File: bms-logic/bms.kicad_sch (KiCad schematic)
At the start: 63 parts, among them J4 Conn_02x07_Odd_Even, Q1 PBSS4350T,215, Q2 BSS123, Q3 DMZ6012E, Q4 DMZ6012E, U11 A2001WR-S-12PD01, U12 A2001WR-S-08PD01, U2 BQ76972PFBR, U3 2SC2383_C41375137, U4 XC6206P332MR

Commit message: started afe layout
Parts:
- removed D6: SMCJ64CA, PCM_JLCPCB:D_SMC, symbol PCM_JLCPCB-Diodes:TVS-Bi,SMCJ64CA
- added D16, D17: BZT52C75, PCM_JLCPCB:D_SOD-123, symbol PCM_JLCPCB-Diodes:Zener,BZT52C75
- renumbered C14 to C10, C15 to C11, C16 to C12, C17 to C13, C18 to C14, C19 to C15, C20 to C16, C7 to C3, C8 to C4, C9 to C5, C10 to C6, C11 to C7, C12 to C8, C13 to C9, J4 to J2, U11 to U2, U12 to U3, U2 to U4, U3 to U5, U4 to U6
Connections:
- net AFE_BAT: now also D16.1
- net GND: now also D17.1
- new net: D16.2, D17.2
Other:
- removed sheet BALANCE
- removed sheet BALANCE1
- added sheet BALANCE15 (balance.kicad_sch)
- added sheet BALANCE16 (balance.kicad_sch)

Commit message: isolated comms
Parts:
- removed U2: A2001WR-S-12PD01, JLCImport:A2001WR-S-12PD01, symbol JLCImport:A2001WR-S-12PD01
- removed U3: A2001WR-S-08PD01, JLCImport:A2001WR-S-08PD01, symbol JLCImport:A2001WR-S-08PD01
- added CN1: S12B-ZR-SM4A-TF, Connector_JST:JST_ZH_S12B-ZR-SM4A-TF_1x12-1MP_P1.50mm_Horizontal, symbol JLCImport:S12B-ZR-SM4A-TF
- added U2: S8B-ZR-SM4A-TF_LF_SN, Connector_JST:JST_ZH_S8B-ZR-SM4A-TF_1x08-1MP_P1.50mm_Horizontal, symbol JLCImport:S8B-ZR-SM4A-TF_LF_SN
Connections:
- net Cell0: now also CN1.2
- net Cell1: now also U2.1
- net Cell10: now also CN1.7
- net Cell11: now also U2.6
- net Cell12: now also CN1.8
- net Cell13: now also U2.7
- net Cell14: now also CN1.9
- net Cell15: now also U2.8
- net Cell16: now also CN1.10
- net Cell2: now also CN1.3
- net Cell3: now also U2.2
- net Cell4: now also CN1.4
- net Cell5: now also U2.3
- net Cell6: now also CN1.5
- net Cell7: now also U2.4
- net Cell8: now also CN1.6
- net Cell9: now also U2.5
- net GND: now also CN1.1, CN1.13, CN1.14, U2.10, U2.9
- net TOP_CELL: now also CN1.11
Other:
- note added: "make these smaller"

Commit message: diagonal
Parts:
- CN1: footprint Connector_JST:JST_ZH_S12B-ZR-SM4A-TF_1x12-1MP_P1.50mm_Horizontal -> JLCImport:JST_ZH_S12B-ZR-SM4A-TF_1x12-1MP_P1.50mm_Horizontal
- U2: footprint Connector_JST:JST_ZH_S8B-ZR-SM4A-TF_1x08-1MP_P1.50mm_Horizontal -> JLCImport:JST_ZH_S8B-ZR-SM4A-TF_1x08-1MP_P1.50mm_Horizontal
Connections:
- net Cell0: now also CN1.11; no longer CN1.2
- net Cell1: now also U2.8; no longer U2.1
- net Cell10: now also CN1.6; no longer CN1.7
- net Cell11: now also U2.3; no longer U2.6
- net Cell12: now also CN1.5; no longer CN1.8
- net Cell13: now also U2.2; no longer U2.7
- net Cell14: now also CN1.4; no longer CN1.9
- net Cell15: now also U2.1; no longer U2.8
- net Cell16: now also CN1.3; no longer CN1.10
- net Cell2: now also CN1.10; no longer CN1.3
- net Cell3: now also U2.7; no longer U2.2
- net Cell4: now also CN1.9; no longer CN1.4
- net Cell5: now also U2.6; no longer U2.3
- net Cell6: now also CN1.8; no longer CN1.5
- net Cell7: now also U2.5; no longer U2.4
- net Cell8: now also CN1.7; no longer CN1.6
- net Cell9: now also U2.4; no longer U2.5
- net GND: now also CN1.12; no longer CN1.1
- net TOP_CELL: now also CN1.2; no longer CN1.11
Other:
- removed sheet THERMISTOR_HEADER2
- removed sheet THERMISTOR_HEADER3
- sheet THERMISTOR_HEADER ports: added THERMISTOR_CHANNEL_A, THERMISTOR_CHANNEL_B; removed THERMISTOR_CHANNEL
- sheet THERMISTOR_HEADER1 ports: added THERMISTOR_CHANNEL_A, THERMISTOR_CHANNEL_B; removed THERMISTOR_CHANNEL

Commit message: kicad 10.0.1 before update to .2
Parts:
- removed D16, D17: BZT52C75, PCM_JLCPCB:D_SOD-123, symbol PCM_JLCPCB-Diodes:Zener,BZT52C75
- removed J2: Conn_02x07_Odd_Even, symbol Connector_Generic:Conn_02x07_Odd_Even
- added CN4: HX_JN1_27-2X10_TP_H4_9, JLCImport:HX_JN1_27-2X10_TP_H4_9, symbol JLCImport:HX_JN1_27-2X10_TP_H4_9
- added D16: SMAJ60CA, Diode_SMD:D_SMA, symbol Diode:SMAJ60CA
- added R90: 10kΩ, PCM_JLCPCB:R_0402, symbol PCM_JLCPCB-Resistors:0402,10kΩ
- added TP24: IO8, TestPoint:TestPoint_Pad_D1.0mm, symbol Connector:TestPoint
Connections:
- net AFE_BAT: now also D16.2 (A2)
- net CHARGE_PUMP: now also CN4.5
- net CHG_GATE_CTRL: now also CN4.7
- net CURRENT_SENSE_N: now also CN4.14
- net CURRENT_SENSE_P: now also CN4.12
- net DCHG: now also CN4.8
- net DDSG: now also CN4.6
- net DSG_GATE_CONTROL: now also CN4.9
- net FUSE: now also CN4.10
- net GND: now also CN1.MP (13), U2.MP (9), CN4.1, D16.1 (A1), R90.2; no longer CN1.13, CN1.14, U2.10, U2.9
- net PACK/LD: now also CN4.13
- net PDSG_GATE_CTRL: now also CN4.11
- net TEMP_CHG: now also CN4.4
- net TEMP_DSG: now also CN4.2
- net TOP_CELL: now also CN4.3
- net SRP: now reaches C11.1, C12.1, C9.2, R21.2, U4.18 (SRP)
- net SRN: now reaches C10.1, C11.2, C12.2, R22.2, U4.20 (SRN)
- net REG18: now reaches C8.1, U4.24 (REG18)
- net at U4.33 (RST_SHUT): now also R90.1, TP24.1
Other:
- moved on the sheet: U2

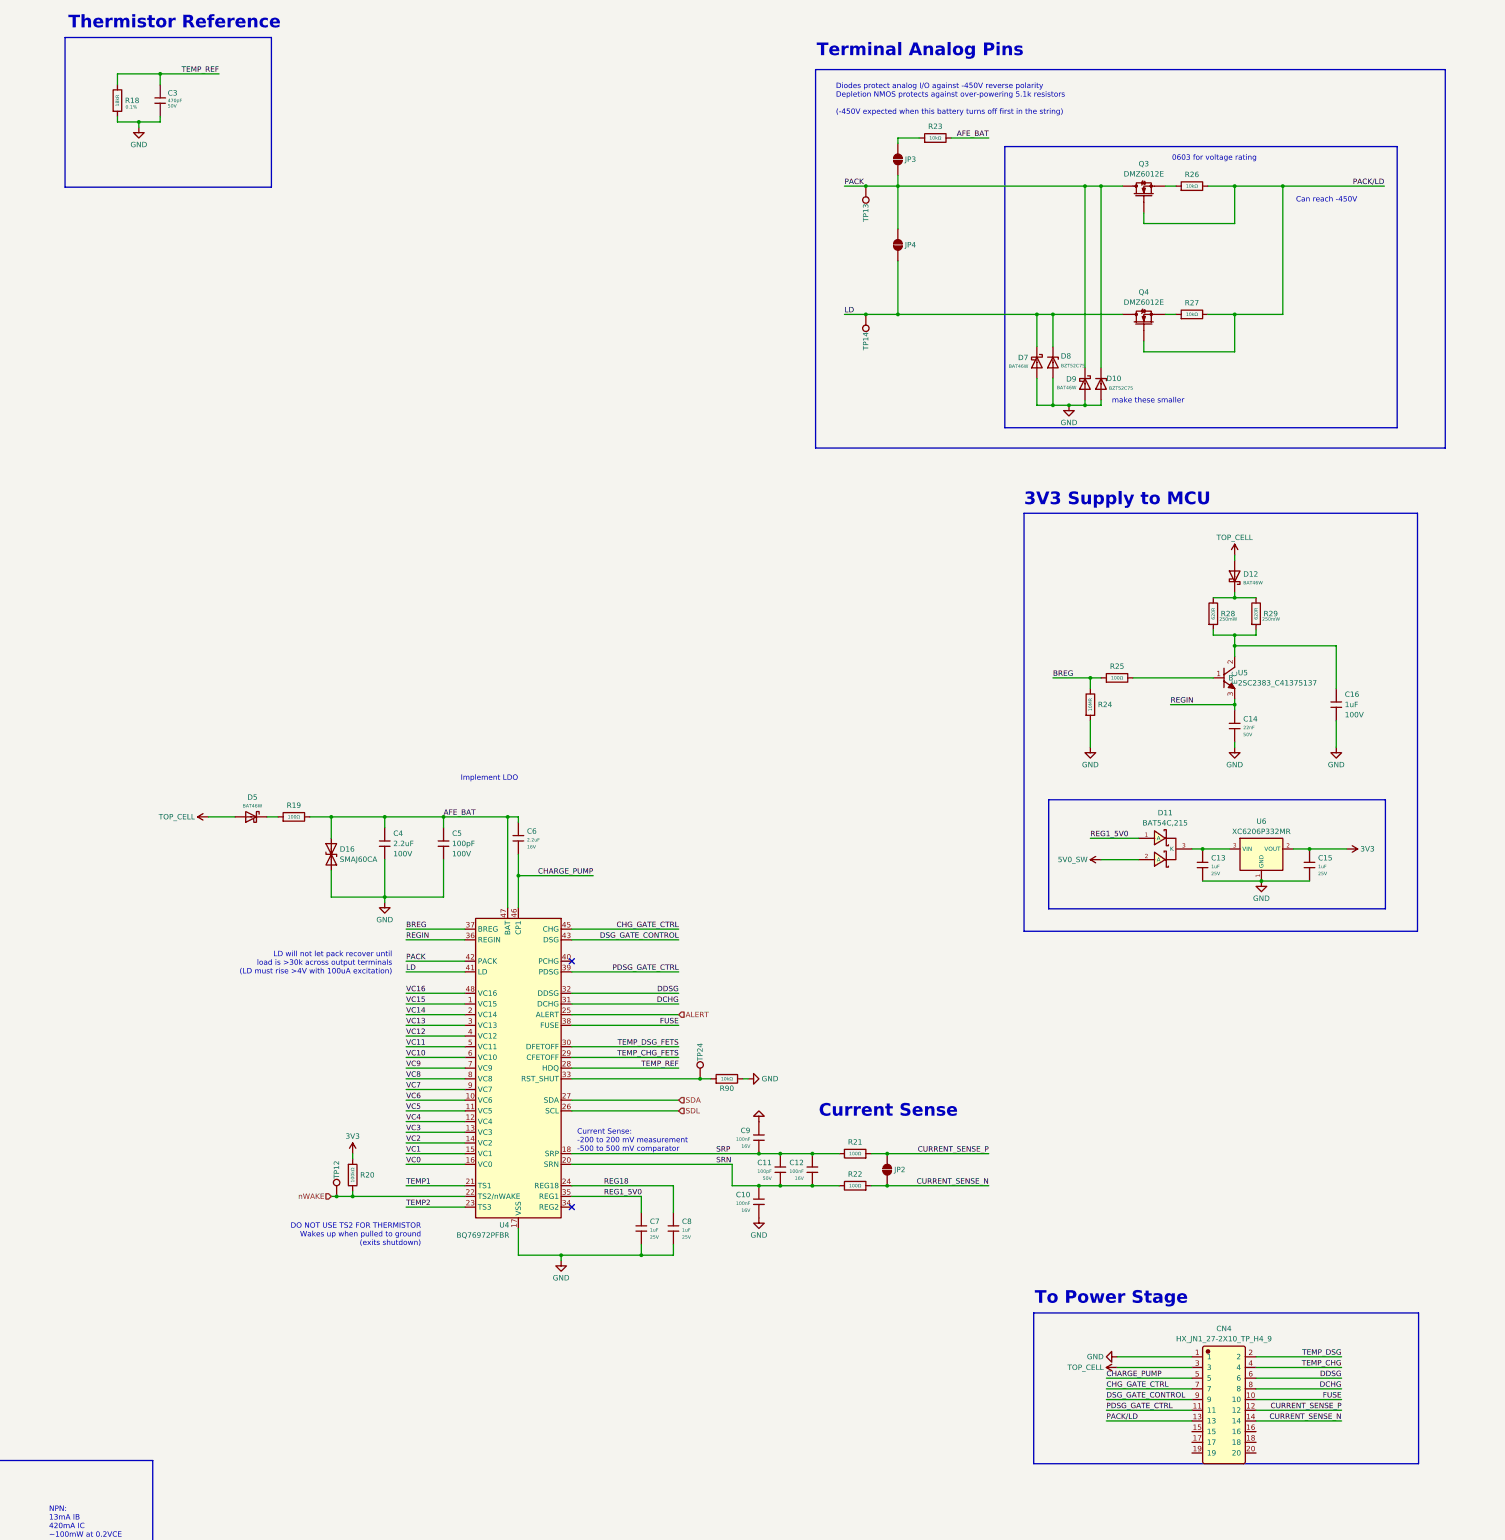
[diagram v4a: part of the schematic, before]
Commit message: more layout, removed some unnecessary features
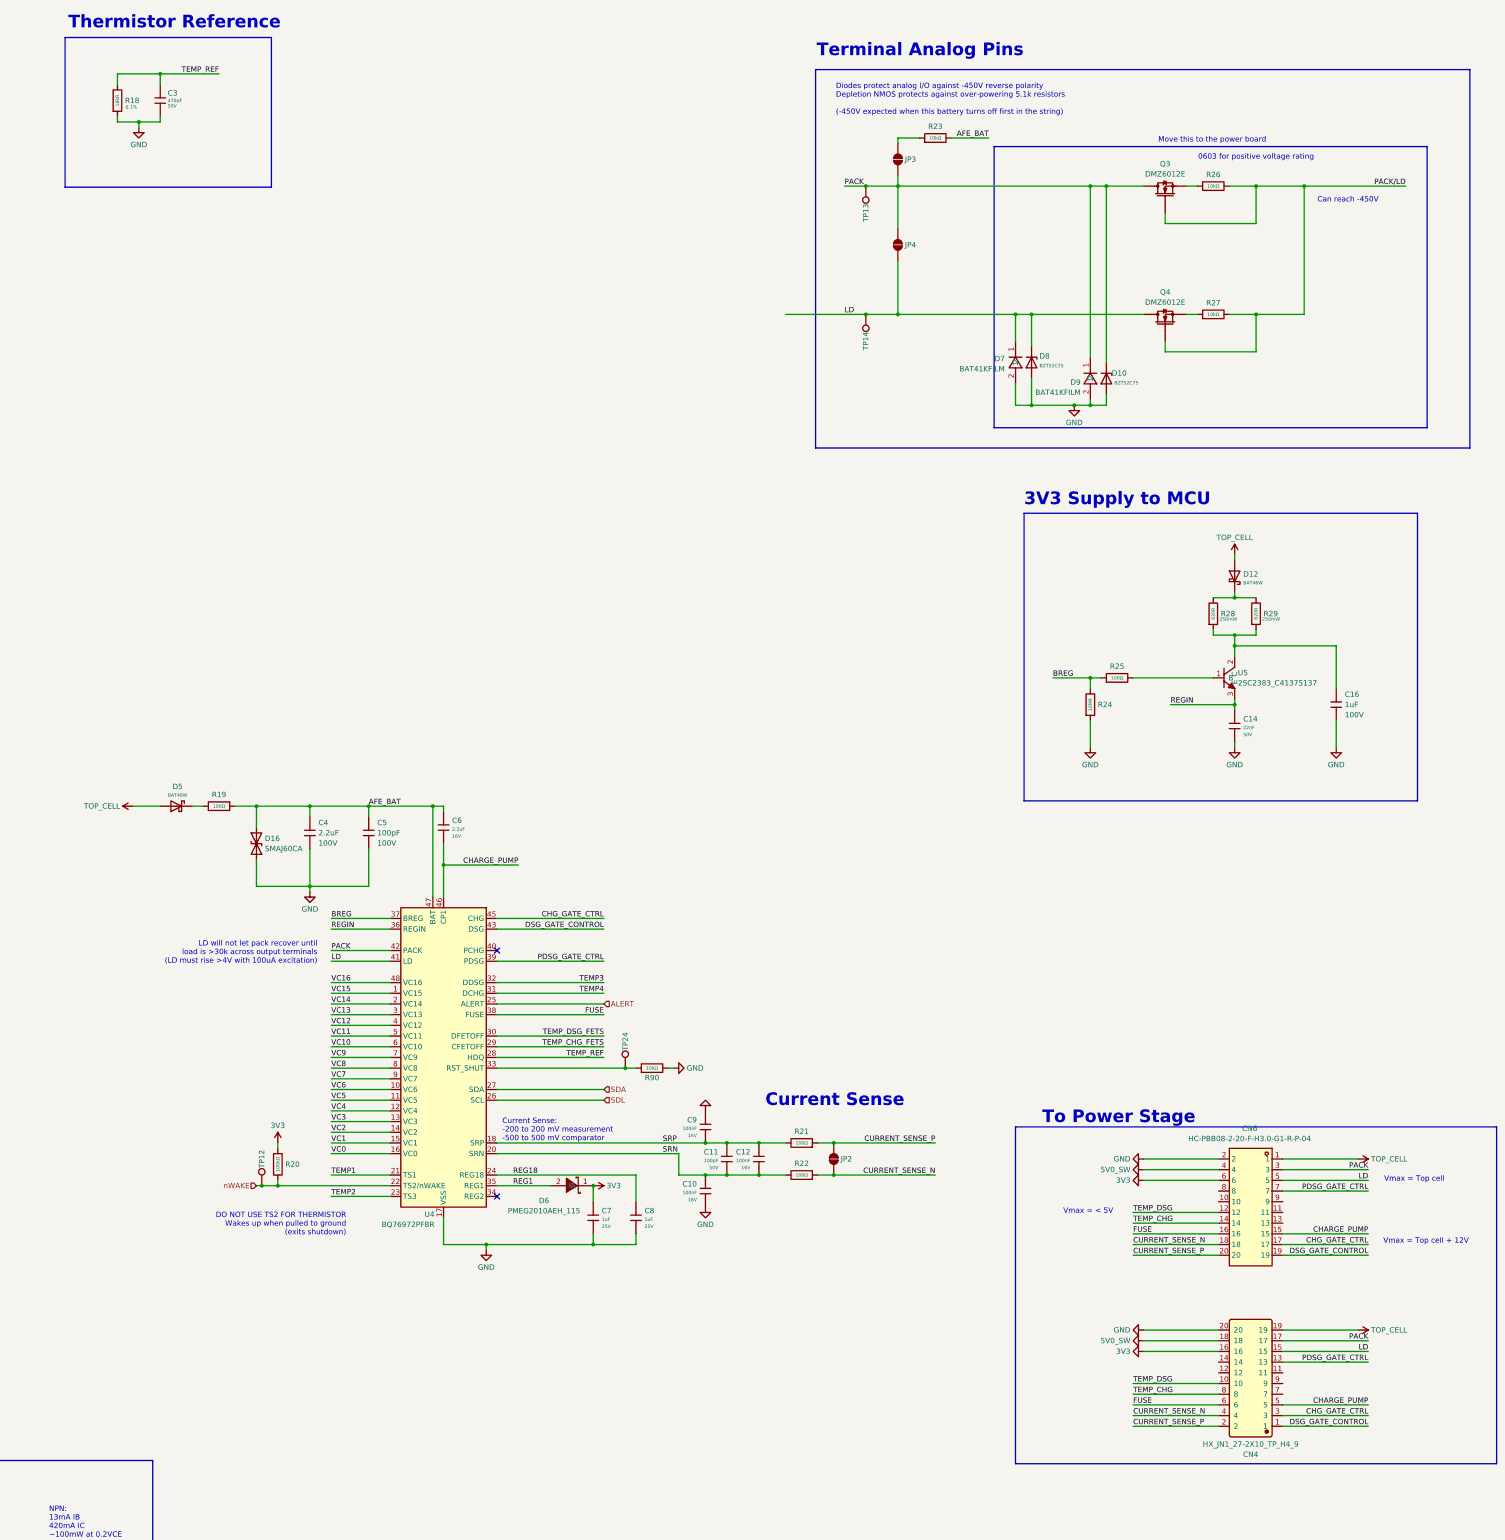
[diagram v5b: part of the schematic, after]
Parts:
- removed C13, C15: 1uF, PCM_JLCPCB:C_0402, symbol PCM_JLCPCB-Capacitors:0402,1uF
- removed D11: BAT54C,215, PCM_JLCPCB:SOT-23-3_L2.9-W1.6-P1.90-LS2.8-BR, symbol PCM_JLCPCB-Diode-Packages:Schottky, BAT54C,215
- removed D7, D9: BAT46W, PCM_JLCPCB:D_SOD-123, symbol PCM_JLCPCB-Diodes:Schottky,BAT46W
- removed U6: XC6206P332MR, PCM_JLCPCB:SOT-23-3_L2.9-W1.6-P1.90-LS2.8-BR, symbol PCM_JLCPCB-Power:LDO, 3.3V, 0.2A
- added CN6: HC-PBB08-2-20-F-H3.0-G1-R-P-04, easyeda2kicad:CONN-SMD_20P-P0.80_HC-PBB08-2-20-F-H4.0-G1-R-P-04, symbol easyeda2kicad:HC-PBB08-2-20-F-H3.0-G1-R-P-04
- added D6: PMEG2010AEH_115, PCM_JLCPCB:D_SOD-123FL, symbol JLCImport:PMEG2010AEH_115
- added D7, D9: BAT41KFILM, PCM_JLCPCB:D_SOD-523, symbol JLCImport:BAT41KFILM
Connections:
- net 3V3: now also C7.1, CN4.16, CN6.6, D6.1 (K)
- net 5V0_SW: now also CN4.18, CN6.4
- net CHARGE_PUMP: now also CN6.15
- net CHG_GATE_CTRL: now also CN4.3, CN6.17; no longer CN4.7
- net CURRENT_SENSE_N: now also CN4.4, CN6.18; no longer CN4.14
- net CURRENT_SENSE_P: now also CN4.2, CN6.20; no longer CN4.12
- net DSG_GATE_CONTROL: now also CN4.1, CN6.19; no longer CN4.9
- net FUSE: now also CN4.6, CN6.16; no longer CN4.10
- net GND: now also CN4.20, CN6.2, D7.2, D9.2; no longer CN4.1
- net LD: now also CN4.15, CN6.5, D7.1
- net PACK: now also CN4.17, CN6.3, D9.1
- net PACK/LD: no longer CN4.13
- net PDSG_GATE_CTRL: now also CN4.13, CN6.7; no longer CN4.11
- net TEMP_CHG: now also CN4.8, CN6.14; no longer CN4.4
- net TEMP_DSG: now also CN4.10, CN6.12; no longer CN4.2
- net TOP_CELL: now also CN4.19, CN6.1; no longer CN4.3
- net DCHG renamed TEMP4
- net TEMP4: no longer CN4.8
- net DDSG renamed TEMP3
- net TEMP3: no longer CN4.6
- net REG1_5V0 renamed REG1
- net REG1: now also D6.2 (A); no longer C7.1
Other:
- note added: "0603 for positive voltage rating"
- note added: "Move this to the power board"
- note added: "Vmax = < 5V"
- note added: "Vmax = Top cell"
- note added: "Vmax = Top cell + 12V"
- note removed: "0603 for voltage rating"
- note removed: "Implement LDO"
- note removed: "make these smaller"
- moved on the sheet: C10, C11, C12, C4, C5, C6, C7, C8, C9, CN4, D10, D16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

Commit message: done with layout, need to address some DRC
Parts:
- added C52, C53: 470pF, PCM_JLCPCB:C_0402, symbol PCM_JLCPCB-Capacitors:0402,470pF
- renumbered U2 to CN2, CN4 to CN5
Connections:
- net TEMP1 is gone; now on net TEMP_CELLS_4: U4.21 (TS1)
- net TEMP2 is gone; now on net TEMP_CELLS_3: U4.23 (TS3)
- net TEMP3 is gone; now on net TEMP_CELLS_2: U4.32 (DDSG)
- net TEMP4 is gone; now on net TEMP_CELLS_1: U4.31 (DCHG)
- net TEMP_CHG is gone; now on net TEMP_CHG_FETS: CN5.8, CN6.14
- net TEMP_DSG is gone; now on net TEMP_DSG_FETS: CN5.10, CN6.12
- net 3V3: no longer C7.1
- net CHARGE_PUMP: now also CN5.1, CN6.19; no longer CN5.5, CN6.15
- net DSG_GATE_CONTROL: now also CN5.5, CN6.15; no longer CN5.1, CN6.19
- net FUSE: no longer CN5.6, CN6.16
- net GND: now also C52.2, C53.2
- net REG1: now also C7.1
- net TEMP_CHG_FETS: now also C53.1
- net TEMP_DSG_FETS: now also C52.1
- net CHG_GATE_CTRL renamed CHG_GATE_CONTROL
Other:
- note added: "change sch symbool to CN?"
- moved on the sheet: R90, TP24
